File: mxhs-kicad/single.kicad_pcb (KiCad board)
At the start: 2 copper layers, 16.5 x 15.9 mm, 6 parts, among them J1 Conn_01x01, J2 Conn_01x01, J3 Conn_01x01, J4 Conn_01x01

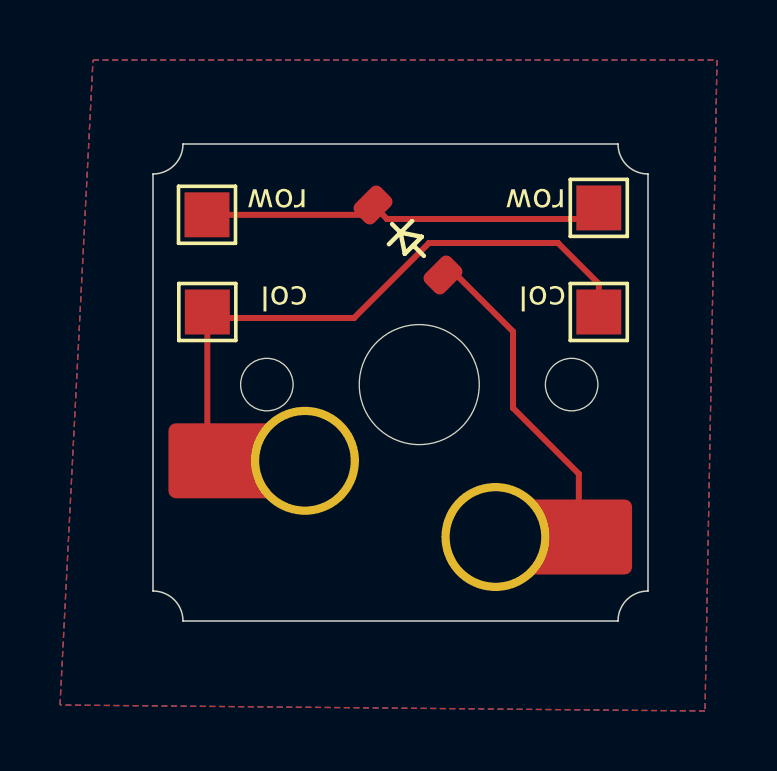
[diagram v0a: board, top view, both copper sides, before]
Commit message: increase sizing to fit behind a cutout
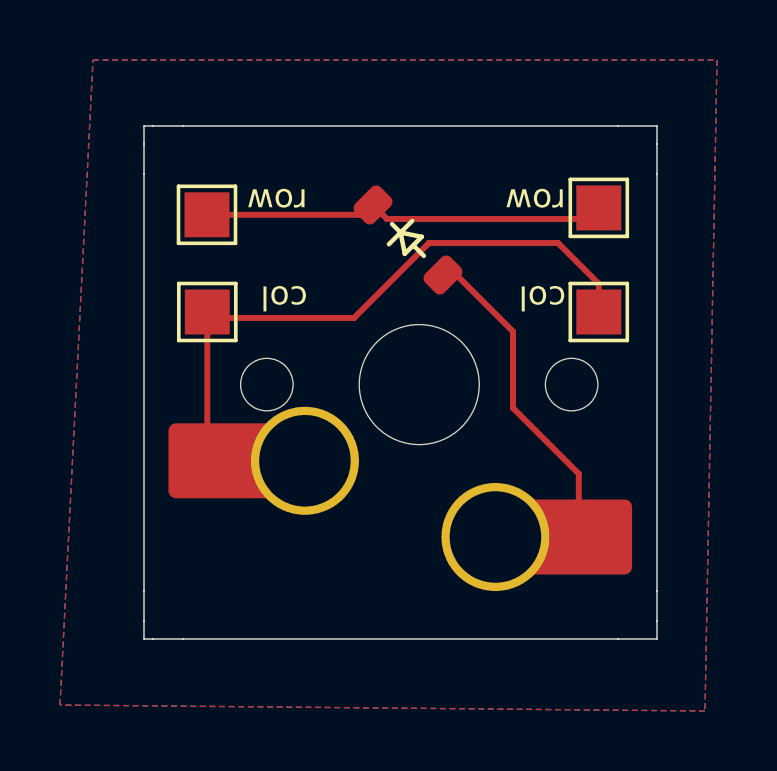
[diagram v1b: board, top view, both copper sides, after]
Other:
- board size 16.5 x 15.9 mm -> 17.1 x 17.1 mm
- board text added: "mxhs"
- board text removed: "beeman mxhss"
